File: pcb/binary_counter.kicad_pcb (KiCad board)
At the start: 2 copper layers, 63.5 x 25.4 mm, 29 parts, among them IC1 ATXMEGA256A3BU-A, J1 Conn_01x02_Male, J2 CONN_02X03, J3 CONN_01X03, SW1 SW_SPDT

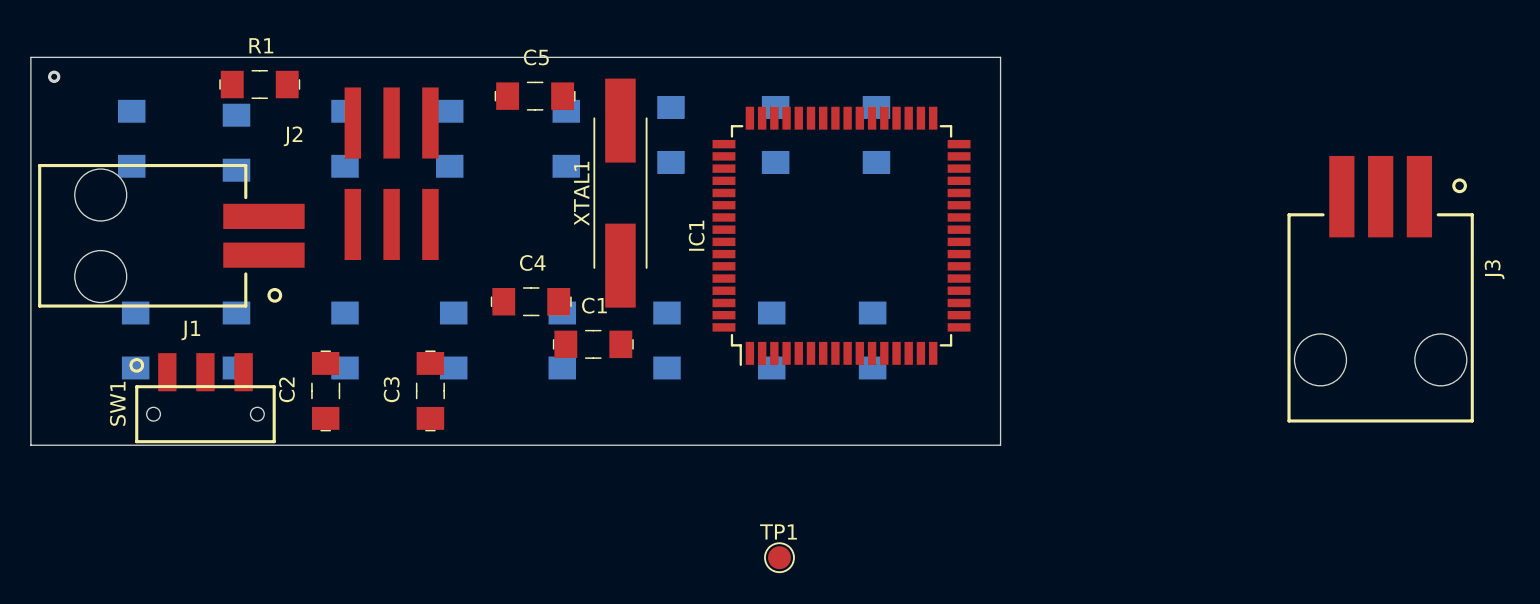
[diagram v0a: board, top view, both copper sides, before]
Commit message: continued PCB layout, all components in appropriate locations now
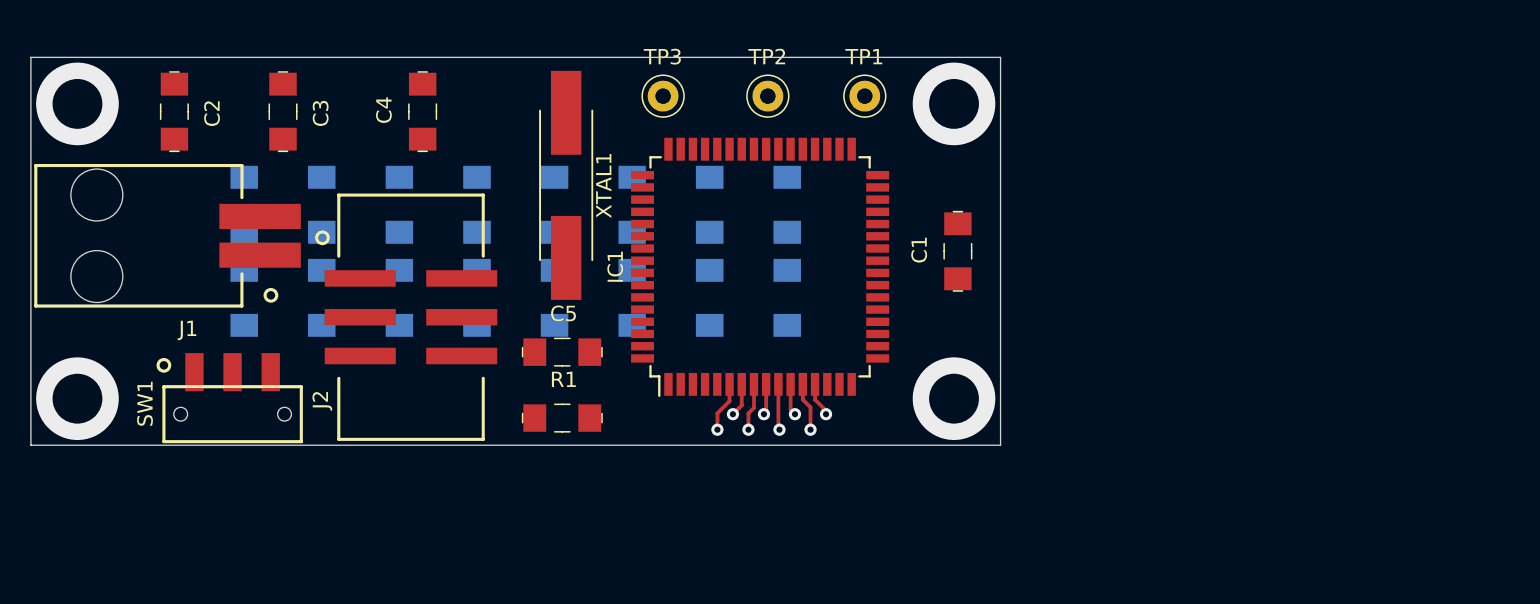
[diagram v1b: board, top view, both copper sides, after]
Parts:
- removed J3: CONN_01X03, binary_counter_footprints:Molex_15_91_2035
- added TP2: 5000, digikey-footprints:Test_Point_D1.02mm, F.Cu at (148.6, 104.1)
- added TP3: 5000, digikey-footprints:Test_Point_D1.02mm, F.Cu at (141.7, 104.1)
- TP1: value TestPoint -> 5000; footprint TestPoint:TestPoint_Pad_D1.5mm -> digikey-footprints:Test_Point_D1.02mm
- moved R9 44.2 mm to (149.9, 117.3), turned to 270 degrees
- moved D8 43.6 mm to (149.9, 111.3), turned to 270 degrees
- moved R2 42.8 mm to (114.3, 117.3), turned to 270 degrees
- moved D1 42.1 mm to (114.3, 111.3), turned to 270 degrees
- moved R8 32.6 mm to (144.8, 117.3), turned to 270 degrees
- moved D7 32.2 mm to (144.8, 111.3), turned to 270 degrees
- moved R3 31.6 mm to (119.4, 117.3), turned to 270 degrees
- moved D2 30.8 mm to (119.4, 111.3), turned to 270 degrees
- moved TP1 30.7 mm to (154.9, 104.1)
- moved R1 29.5 mm to (135.1, 125.2)
- moved C1 24.6 mm to (161.0, 114.3), turned to 90 degrees
- moved R7 21.5 mm to (139.7, 117.3), turned to 270 degrees
- moved C2 20.8 mm to (109.7, 105.2), turned to 270 degrees
- moved D6 20.8 mm to (139.7, 111.3), turned to 270 degrees
- moved R4 20.7 mm to (124.5, 117.3), turned to 270 degrees
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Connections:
- C1 pad 1: +3V3 -> +3V0
- IC1 pad 15: +3V3 -> +3V0
- IC1 pad 25: +3V3 -> +3V0
- IC1 pad 35: +3V3 -> +3V0
- IC1 pad 45: +3V3 -> +3V0
- IC1 pad 53: +3V3 -> +3V0
- IC1 pad 61: +3V3 -> +3V0
- J2 pad 2: +3V3 -> +3V0
- TP1 pad 1: Net-(IC1-Pad62) -> Net-(IC1-Pad38)
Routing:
- net Net-(IC1-Pad6): track 0.00 -> 3.55 mm, vias 0 -> 1
- net Net-(IC1-Pad12): track 0.00 -> 3.43 mm, vias 0 -> 1
- net Net-(IC1-Pad8): track 0.00 -> 3.37 mm, vias 0 -> 1
- net Net-(IC1-Pad10): track 0.00 -> 3.25 mm, vias 0 -> 1
- net Net-(IC1-Pad13): track 0.00 -> 2.25 mm, vias 0 -> 1
- net Net-(IC1-Pad7): track 0.00 -> 2.19 mm, vias 0 -> 1
- net Net-(IC1-Pad11): track 0.00 -> 2.07 mm, vias 0 -> 1
- net Net-(IC1-Pad9): track 0.00 -> 2.01 mm, vias 0 -> 1
- net GND: vias 0 -> 4
- net (no net): vias 1 -> 0

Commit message: finished first pass at pcb layout
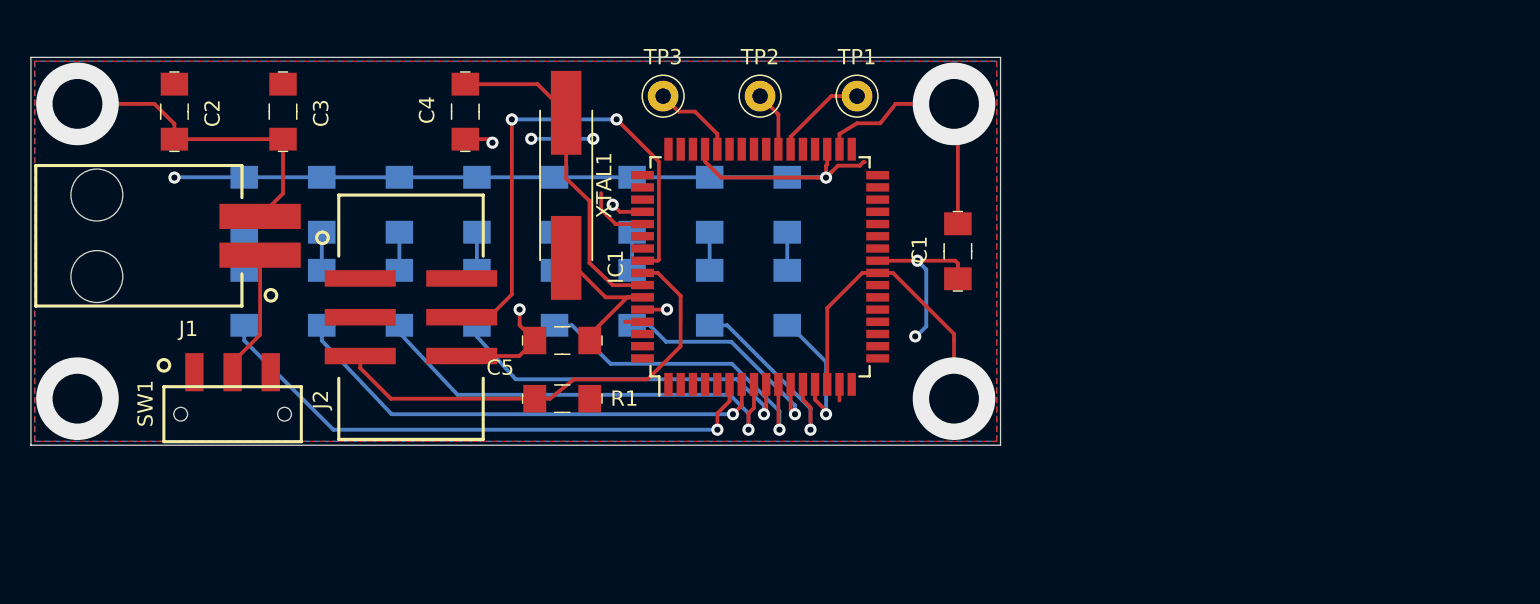
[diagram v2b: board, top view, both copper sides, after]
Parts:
- moved C4 2.79 mm to (128.8, 105.2)
- moved R1 1.27 mm to (135.1, 124.0)
- moved C5 0.76 mm to (135.1, 120.1)
- moved TP1 0.51 mm to (154.4, 104.1)
- moved TP2 0.51 mm to (148.1, 104.1)
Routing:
- net +3V0: track 0.00 -> 79.6 mm, vias 0 -> 6
- net GND: track 0.00 -> 76.9 mm, vias 4 -> 8
- net Net-(IC1-Pad6): track 3.55 -> 38.0 mm
- net Net-(IC1-Pad56): track 0.00 -> 33.9 mm, vias 0 -> 2
- net Net-(IC1-Pad57): track 0.00 -> 30.4 mm
- net Net-(IC1-Pad7): track 2.19 -> 32.2 mm
- net Net-(IC1-Pad8): track 3.37 -> 30.1 mm
- net Net-(IC1-Pad9): track 2.01 -> 24.0 mm
- net Net-(C4-Pad2): track 0.00 -> 21.9 mm
- net Net-(IC1-Pad10): track 3.25 -> 21.5 mm
- net Net-(IC1-Pad11): track 2.07 -> 15.5 mm
- net Net-(C5-Pad2): track 0.00 -> 12.7 mm
- net Net-(IC1-Pad12): track 3.43 -> 13.7 mm
- net Net-(J1-Pad1): track 0.00 -> 8.41 mm
- net Net-(IC1-Pad13): track 2.25 -> 9.21 mm
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- added copper zone on F.Cu, net +3V0
- added copper zone on B.Cu, net GND

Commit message: tweaked pcb layout, passes default drc
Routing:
- net +3V0: track 79.6 -> 83.9 mm
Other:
- board text added: "binary counter v1.0 thayer school of engineering m.kokko - 6/2019"

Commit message: updated drcs
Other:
- rule trace_min: 0.2 -> 0.1524
- rule via_min_drill: 0.3 -> 0.254
- rule via_min_size: 0.4 -> 0.508
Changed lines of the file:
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@@
     (zone_clearance 0.508)
     (zone_45_only no)
-    (trace_min 0.2)
+    (trace_min 0.1524)
     (via_size 0.8)
     (via_drill 0.4)
-    (via_min_size 0.4)
-    (via_min_drill 0.3)
-    (uvia_size 0.3)
-    (uvia_drill 0.1)
+    (via_min_size 0.508)
+    (via_min_drill 0.254)
+    (uvia_size 0.508)
+    (uvia_drill 0.254)
     (uvias_allowed no)
-    (uvia_min_size 0.2)
-    (uvia_min_drill 0.1)
+    (uvia_min_size 0.4826)
+    (uvia_min_drill 0.2286)
     (edge_width 0.05)
     (segment_width 0.2)
@@
     (via_dia 0.8)
     (via_drill 0.4)
-    (uvia_dia 0.3)
-    (uvia_drill 0.1)
+    (uvia_dia 0.508)
+    (uvia_drill 0.254)
     (add_net +3V0)
     (add_net GND)
@@
   (gr_line (start 163.83 101.6) (end 163.83 127) (layer Edge.Cuts) (width 0.05))
   (gr_line (start 100.33 101.6) (end 163.83 101.6) (layer Edge.Cuts) (width 0.05))
-  (segment (start 154.94 122.174) (end 154.178 121.412) (width 0.25) (layer F.Cu) (net 2))
-  (segment (start 154.94 122.174) (end 155.702 122.936) (width 0.25) (layer F.Cu) (net 2))
   (via (at 103.378 104.648) (size 5.4102) (drill 3.2639) (layers F.Cu B.Cu) (net 1))
   (via (at 103.378 123.952) (size 5.4102) (drill 3.2639) (layers F.Cu B.Cu) (net 1))
@@
   (segment (start 138.894 111.716) (end 138.43 111.252) (width 0.25) (layer F.Cu) (net 1))
   (segment (start 140.382 111.716) (end 138.894 111.716) (width 0.25) (layer F.Cu) (net 1))
+  (segment (start 154.94 122.174) (end 154.178 121.412) (width 0.25) (layer F.Cu) (net 2))
+  (segment (start 154.94 122.174) (end 155.702 122.936) (width 0.25) (layer F.Cu) (net 2))
   (segment (start 149.86 109.452) (end 144.78 109.452) (width 0.25) (layer B.Cu) (net 2))
   (segment (start 144.78 109.452) (end 139.7 109.452) (width 0.25) (layer B.Cu) (net 2))
